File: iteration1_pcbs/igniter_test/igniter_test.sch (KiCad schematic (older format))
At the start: 3 parts, among them J1 Conn_01x02, U1 Teensy4.0

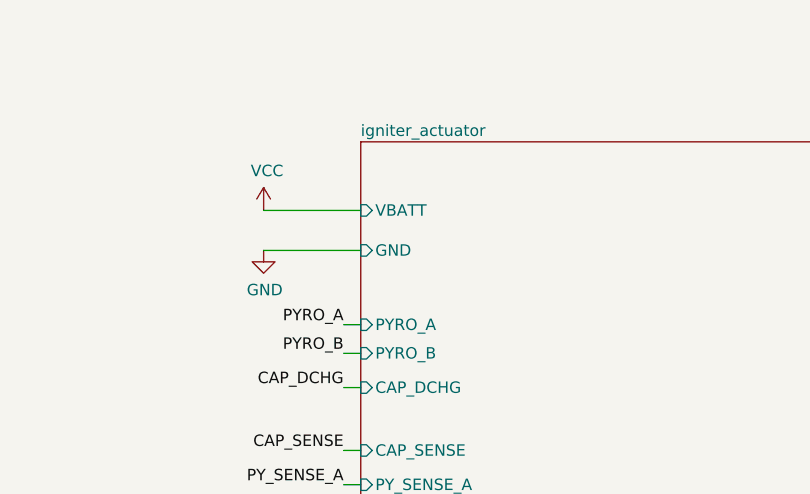
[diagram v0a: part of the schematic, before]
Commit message: Adding igniter testing
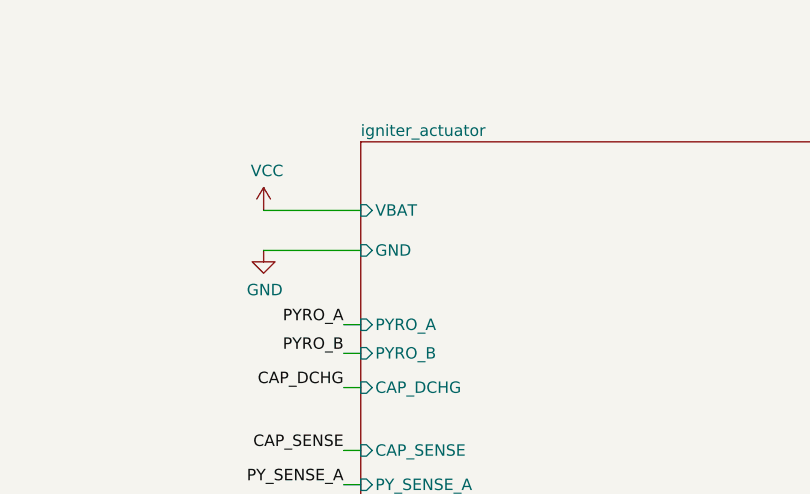
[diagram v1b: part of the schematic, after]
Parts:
- TH1: footprint (none) -> iteration1:SL05_4R003
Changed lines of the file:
@@
 F0 "igniter_actuator" 50
 F1 "igniter_actuator.sch" 50
-F2 "VBATT" I L 7775 1875 50
-F3 "GND" I L 7775 2050 50
-F4 "CAP_SENSE" I L 7775 2925 50
-F5 "PYRO_A" I L 7775 2375 50
-F6 "PYRO_B" I L 7775 2500 50
-F7 "CAP_DCHG" I L 7775 2650 50
-F8 "PY_SENSE_A" I L 7775 3075 50
-F9 "PY_SENSE_B" I L 7775 3225 50
+F2 "GND" I L 7775 2050 50
+F3 "CAP_SENSE" I L 7775 2925 50
+F4 "PYRO_A" I L 7775 2375 50
+F5 "PYRO_B" I L 7775 2500 50
+F6 "CAP_DCHG" I L 7775 2650 50
+F7 "PY_SENSE_A" I L 7775 3075 50
+F8 "PY_SENSE_B" I L 7775 3225 50
+F9 "VBAT" I L 7775 1875 50
 $EndSheet
 $Comp
@@
 F 0 "TH1" H 8397 4371 50  0000 L CNN
 F 1 "SL05 4R003" H 8397 4280 50  0000 L CNN
-F 2 "" H 8300 4375 50  0001 C CNN
+F 2 "iteration1:SL05_4R003" H 8300 4375 50  0001 C CNN
 F 3 "~" H 8300 4375 50  0001 C CNN
 	1    8300 4325

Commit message: igniter test tracks
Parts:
- J1: value Conn_01x02 -> XT60
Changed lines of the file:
@@
 P 9400 4025
 F 0 "J1" H 9480 4017 50  0000 L CNN
-F 1 "Conn_01x02" H 9480 3926 50  0000 L CNN
+F 1 "XT60" H 9480 3926 50  0000 L CNN
 F 2 "Connector_AMASS:AMASS_XT60-M_1x02_P7.20mm_Vertical" H 9400 4025 50  0001 C CNN
 F 3 "~" H 9400 4025 50  0001 C CNN

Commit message: Adding most of the changes, almost don
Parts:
- added H1, H2, H3, H4: MountingHole_Pad, MountingHole:MountingHole_3.2mm_M3_Pad_Via, symbol Mechanical:MountingHole_Pad
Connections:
- net GND: now also H1.1, H2.1, H3.1, H4.1
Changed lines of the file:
@@
 Wire Wire Line
 	8300 4675 8300 4475
+$Comp
+L Mechanical:MountingHole_Pad H1
+U 1 1 611B3938
+P 9600 4550
+F 0 "H1" H 9700 4599 50  0000 L CNN
+F 1 "MountingHole_Pad" H 9700 4508 50  0000 L CNN
+F 2 "MountingHole:MountingHole_3.2mm_M3_Pad_Via" H 9600 4550 50  0001 C CNN
+F 3 "~" H 9600 4550 50  0001 C CNN
+	1    9600 4550
+	1    0    0    -1
+$EndComp
+$Comp
+L Mechanical:MountingHole_Pad H2
+U 1 1 611B3F4C
+P 9600 5000
+F 0 "H2" H 9700 5049 50  0000 L CNN
+F 1 "MountingHole_Pad" H 9700 4958 50  0000 L CNN
+F 2 "MountingHole:MountingHole_3.2mm_M3_Pad_Via" H 9600 5000 50  0001 C CNN
+F 3 "~" H 9600 5000 50  0001 C CNN
+	1    9600 5000
+	1    0    0    -1
+$EndComp
+$Comp
+L Mechanical:MountingHole_Pad H3
+U 1 1 611B4927
+P 9600 5475
+F 0 "H3" H 9700 5524 50  0000 L CNN
+F 1 "MountingHole_Pad" H 9700 5433 50  0000 L CNN
+F 2 "MountingHole:MountingHole_3.2mm_M3_Pad_Via" H 9600 5475 50  0001 C CNN
+F 3 "~" H 9600 5475 50  0001 C CNN
+	1    9600 5475
+	1    0    0    -1
+$EndComp
+$Comp
+L Mechanical:MountingHole_Pad H4
+U 1 1 611B63D1
+P 9600 5950
+F 0 "H4" H 9700 5999 50  0000 L CNN
+F 1 "MountingHole_Pad" H 9700 5908 50  0000 L CNN
+F 2 "MountingHole:MountingHole_3.2mm_M3_Pad_Via" H 9600 5950 50  0001 C CNN
+F 3 "~" H 9600 5950 50  0001 C CNN
+	1    9600 5950
+	1    0    0    -1
+$EndComp
+$Comp
+L power:GND #PWR06
+U 1 1 611B7352
+P 9600 4650
+F 0 "#PWR06" H 9600 4400 50  0001 C CNN
+F 1 "GND" H 9605 4477 50  0000 C CNN
+F 2 "" H 9600 4650 50  0001 C CNN
+F 3 "" H 9600 4650 50  0001 C CNN
+	1    9600 4650
+	1    0    0    -1
+$EndComp
+$Comp
+L power:GND #PWR07
+U 1 1 611B759D
+P 9600 5100
+F 0 "#PWR07" H 9600 4850 50  0001 C CNN
+F 1 "GND" H 9605 4927 50  0000 C CNN
+F 2 "" H 9600 5100 50  0001 C CNN
+F 3 "" H 9600 5100 50  0001 C CNN
+	1    9600 5100
+	1    0    0    -1
+$EndComp
+$Comp
+L power:GND #PWR08
+U 1 1 611B77B0
+P 9600 5575
+F 0 "#PWR08" H 9600 5325 50  0001 C CNN
+F 1 "GND" H 9605 5402 50  0000 C CNN
+F 2 "" H 9600 5575 50  0001 C CNN
+F 3 "" H 9600 5575 50  0001 C CNN
+	1    9600 5575
+	1    0    0    -1
+$EndComp
+$Comp
+L power:GND #PWR09
+U 1 1 611B79F1
+P 9600 6050
+F 0 "#PWR09" H 9600 5800 50  0001 C CNN
+F 1 "GND" H 9605 5877 50  0000 C CNN
+F 2 "" H 9600 6050 50  0001 C CNN
+F 3 "" H 9600 6050 50  0001 C CNN
+	1    9600 6050
+	1    0    0    -1
+$EndComp
 $EndSCHEMATC
